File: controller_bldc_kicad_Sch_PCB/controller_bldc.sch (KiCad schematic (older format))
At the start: 55 parts, among them J1 Battery Supply, J2 Emergency Button OUT, J3 Emergency Button IN, J4 Brake, J5 Throttle, J6 LM35, J7 Hall Sensors, J8 Nextion Nx3224T028, J9 BLDC Motor, K1 ADW11, Q1 IRF1010N, Q2 IRF1010N, Q3 IRF1010N, Q4 IRF1010N, Q5 IRF1010N, Q6 IRF1010N, SW1 SW_SPST, SW2 SW_Push, U1 ESP32-DEVKITC-32D, U2 LM317_TO-220, U3 LM7805_TO220, U4 IR2103, U8 IR2103, U9 IR2103

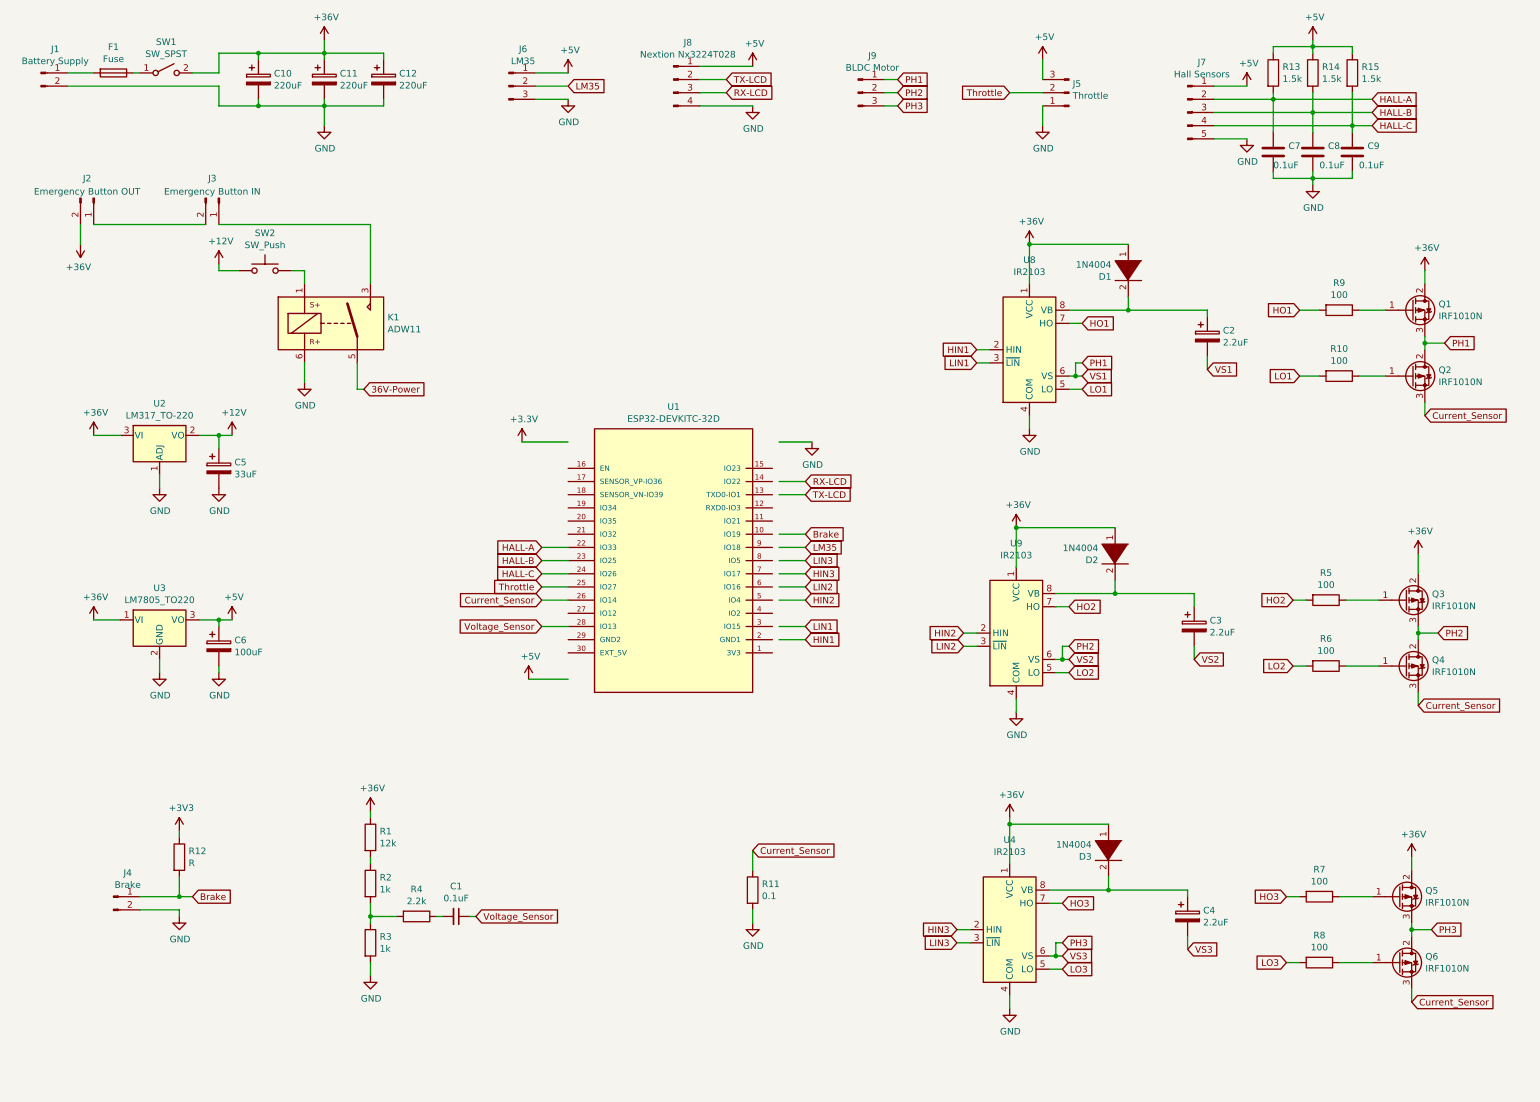
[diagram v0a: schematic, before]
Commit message: PCB in v0.7, only relay to change for next and maybe the first tri
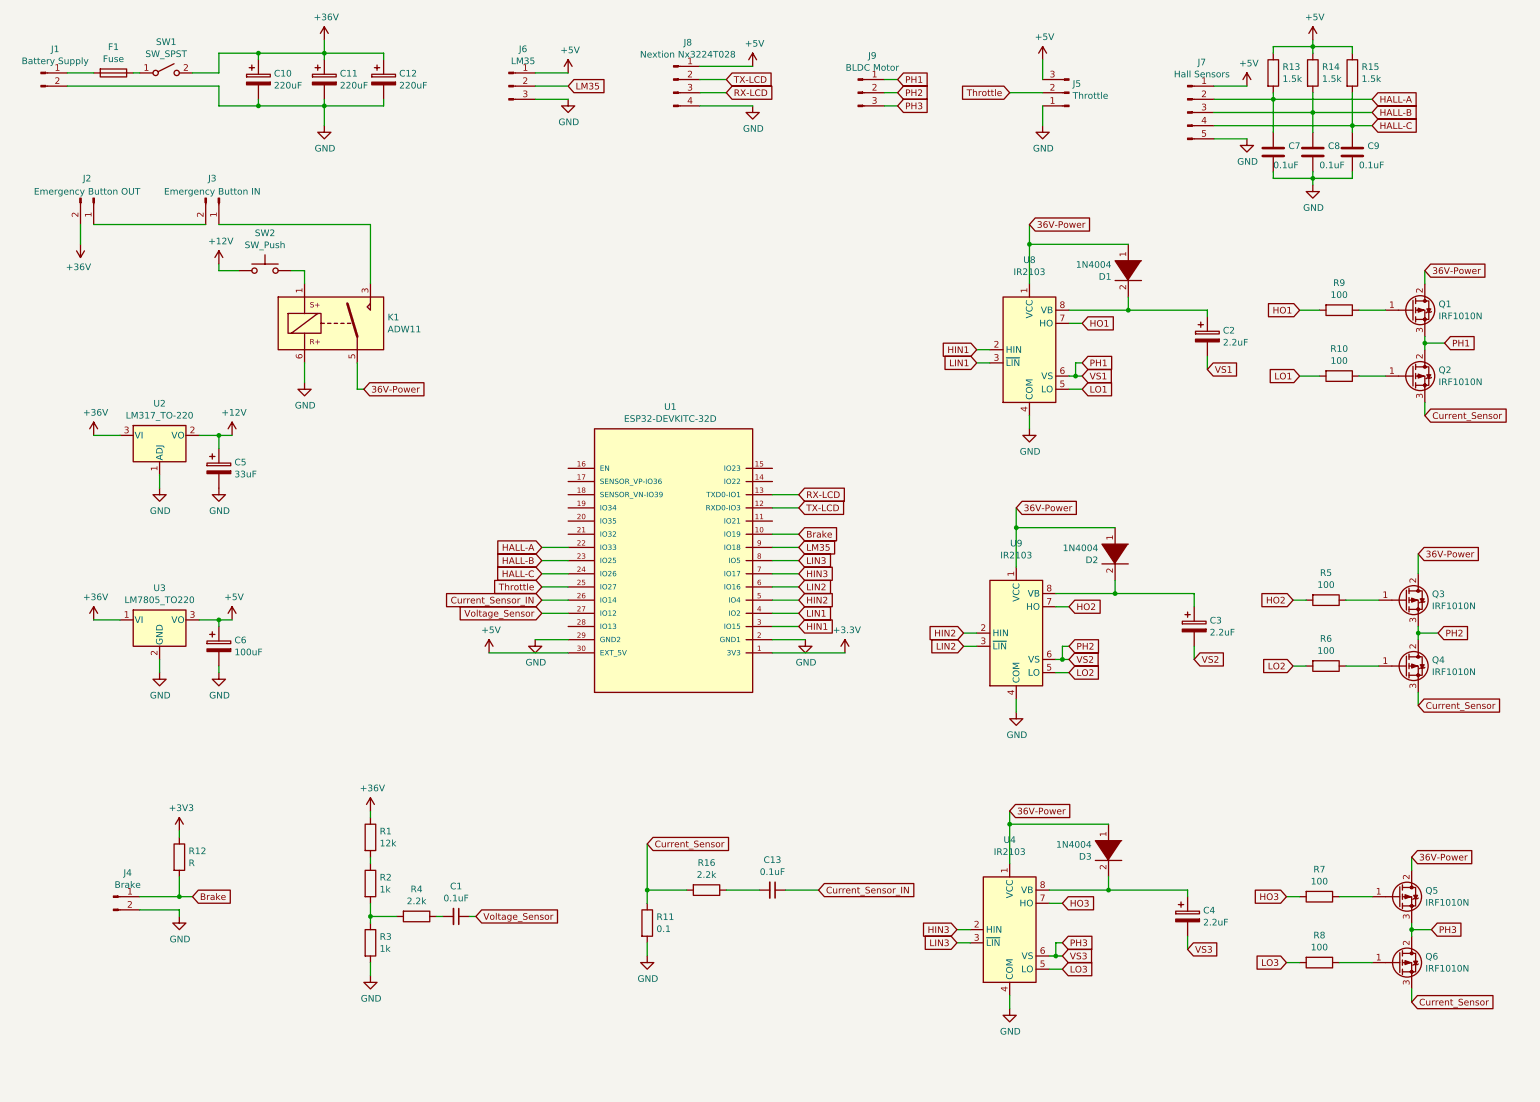
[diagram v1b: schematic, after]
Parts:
- added C13: 0.1uF, Capacitor_THT:C_Disc_D7.5mm_W5.0mm_P10.00mm, symbol Device:C_Small
- added R16: 2.2k, Resistor_THT:R_Axial_DIN0207_L6.3mm_D2.5mm_P10.16mm_Horizontal, symbol Device:R
- U1: footprint MODULE_ESP32-DEVKITC-32D -> ESP32-DEVKITC-32D_Electeam:MODULE_ESP32-DEVKITC-32D
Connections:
- net labels added: Current_Sensor_IN
- wire segments 192 -> 199
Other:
- moved on the sheet: R11

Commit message: V0.8 with everything except for the relay that should consume less current, 36V-Power is fixed.
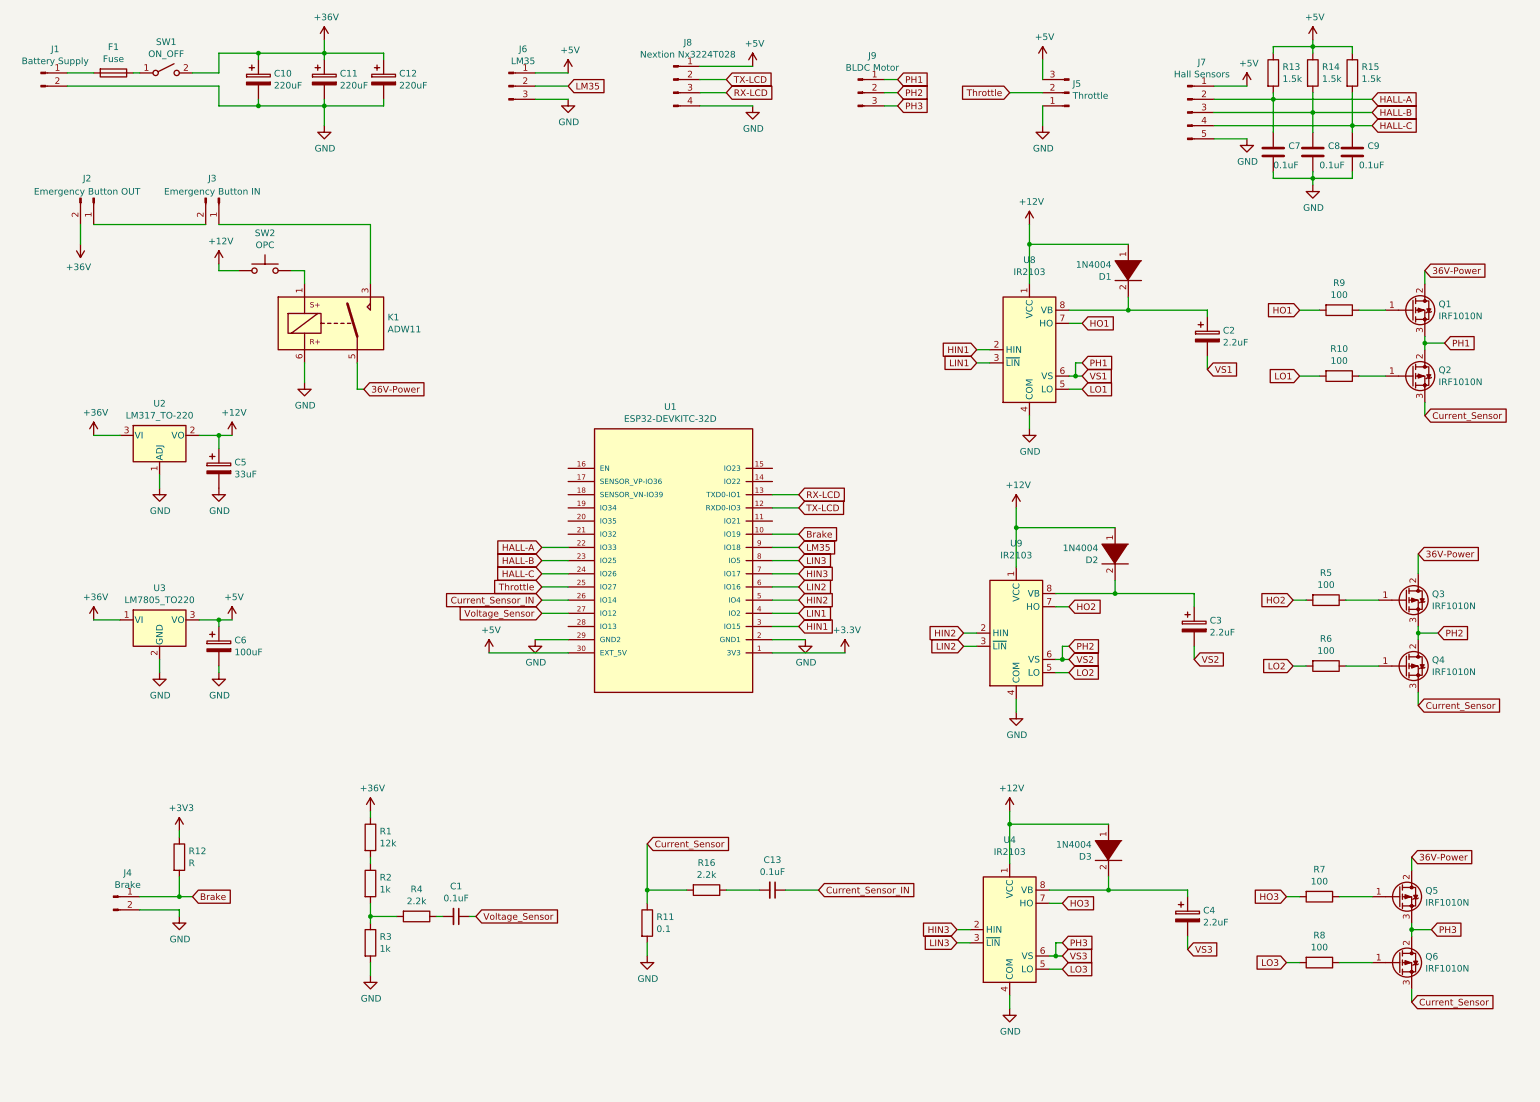
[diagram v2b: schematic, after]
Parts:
- SW1: value SW_SPST -> ON_OFF
- SW2: value SW_Push -> OPC
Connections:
- net +12V: now also D1.1 (K), D2.1 (K), D3.1 (K), U4.1 (VCC), U8.1 (VCC), U9.1 (VCC)
- net 36V-Power: no longer D1.1 (K), D2.1 (K), D3.1 (K), U4.1 (VCC), U8.1 (VCC), U9.1 (VCC)
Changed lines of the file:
@@
 P 1300 500
 F 0 "SW1" H 1300 735 50  0000 C CNN
-F 1 "SW_SPST" H 1300 644 50  0000 C CNN
+F 1 "ON_OFF" H 1300 644 50  0000 C CNN
 F 2 "Connector_Molex:Molex_KK-254_AE-6410-02A_1x02_P2.54mm_Vertical" H 1300 500 50  0001 C CNN
 F 3 "~" H 1300 500 50  0001 C CNN
@@
 P 2050 2000
 F 0 "SW2" H 2050 2285 50  0000 C CNN
-F 1 "SW_Push" H 2050 2194 50  0000 C CNN
+F 1 "OPC" H 2050 2194 50  0000 C CNN
 F 2 "Connector_Molex:Molex_KK-254_AE-6410-02A_1x02_P2.54mm_Vertical" H 2050 2200 50  0001 C CNN
 F 3 "~" H 2050 2200 50  0001 C CNN
@@
 Text GLabel 10850 2000 2    50   Input ~ 0
 36V-Power
-Text GLabel 7850 1650 2    50   Input ~ 0
-36V-Power
-Text GLabel 7750 3800 2    50   Input ~ 0
-36V-Power
 Text GLabel 10800 4150 2    50   Input ~ 0
 36V-Power
 Text GLabel 10750 6450 2    50   Input ~ 0
 36V-Power
-Text GLabel 7700 6100 2    50   Input ~ 0
-36V-Power
 Wire Wire Line
 	7700 6100 7700 6200
-Wire Wire Line
-	7750 3950 7750 3800
 Connection ~ 7750 3950
 Wire Wire Line
@@
 Wire Wire Line
 	6000 6700 6250 6700
+$Comp
+L power:+12V #PWR0115
+U 1 1 608462B9
+P 7850 1650
+F 0 "#PWR0115" H 7850 1500 50  0001 C CNN
+F 1 "+12V" H 7865 1823 50  0000 C CNN
+F 2 "" H 7850 1650 50  0001 C CNN
+F 3 "" H 7850 1650 50  0001 C CNN
+	1    7850 1650
+	1    0    0    -1
+$EndComp
+Wire Wire Line
+	7750 3950 7750 3800
+$Comp
+L power:+12V #PWR0116
+U 1 1 6084A421
+P 7750 3800
+F 0 "#PWR0116" H 7750 3650 50  0001 C CNN
+F 1 "+12V" H 7765 3973 50  0000 C CNN
+F 2 "" H 7750 3800 50  0001 C CNN
+F 3 "" H 7750 3800 50  0001 C CNN
+	1    7750 3800
+	1    0    0    -1
+$EndComp
+$Comp
+L power:+12V #PWR0117
+U 1 1 6084AD2A
+P 7700 6100
+F 0 "#PWR0117" H 7700 5950 50  0001 C CNN
+F 1 "+12V" H 7715 6273 50  0000 C CNN
+F 2 "" H 7700 6100 50  0001 C CNN
+F 3 "" H 7700 6100 50  0001 C CNN
+	1    7700 6100
+	1    0    0    -1
+$EndComp
 $EndSCHEMATC
